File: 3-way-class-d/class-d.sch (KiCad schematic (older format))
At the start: 7 parts

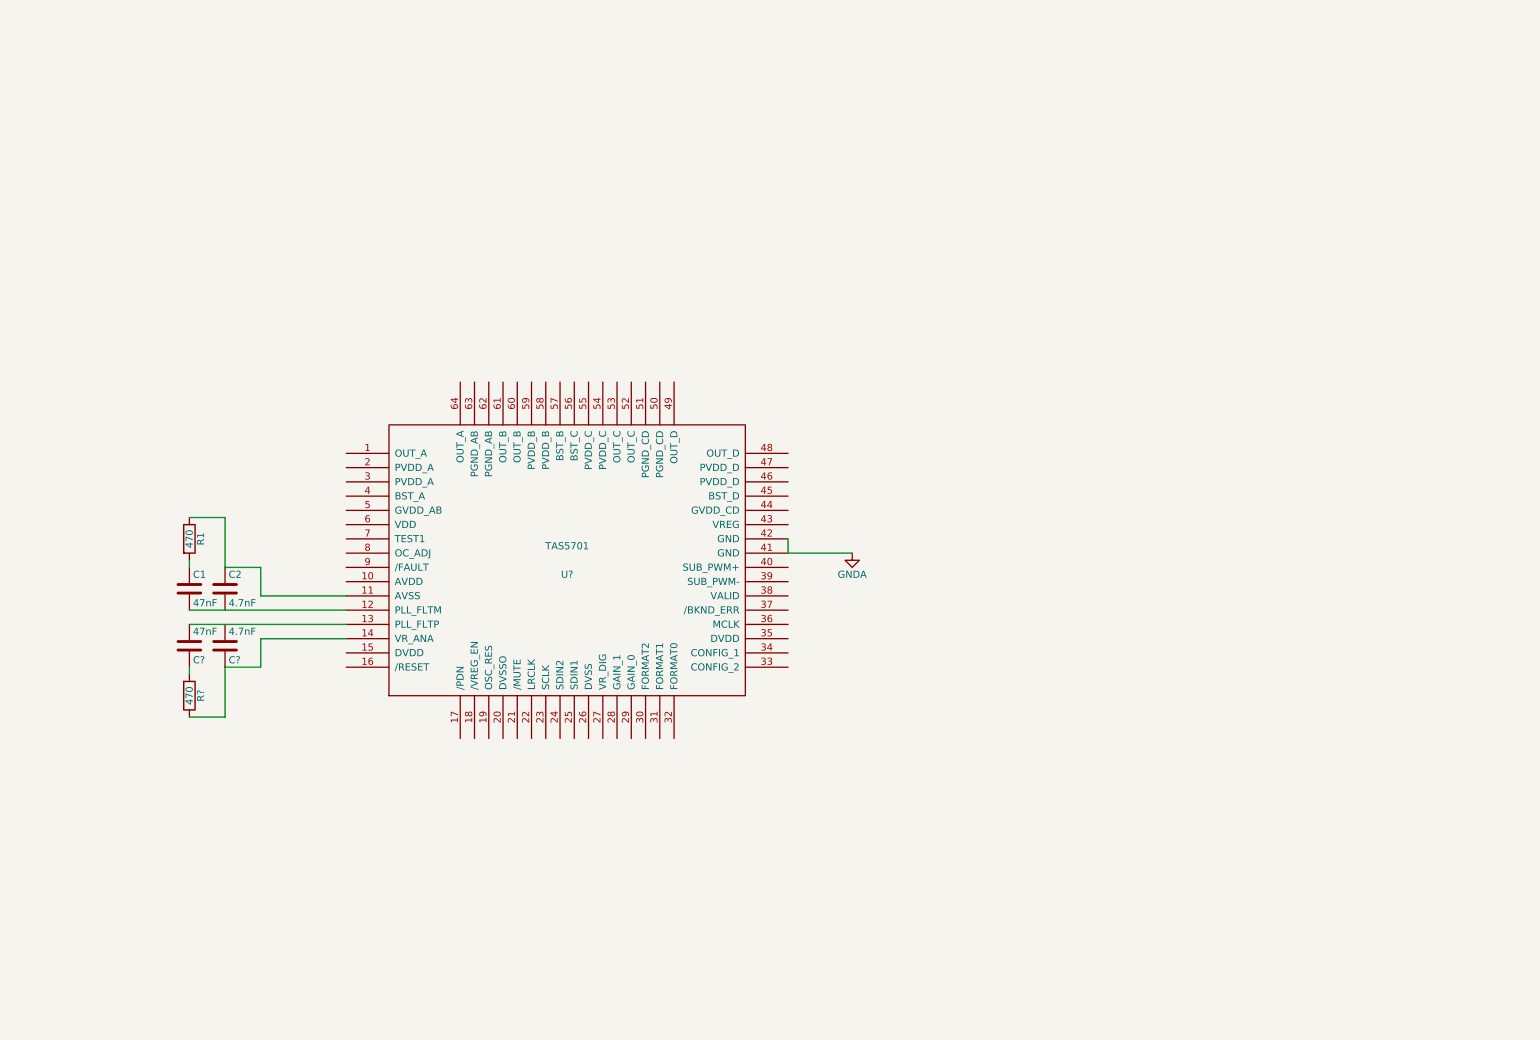
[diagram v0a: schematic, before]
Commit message: Format, gain, fault & mute LED
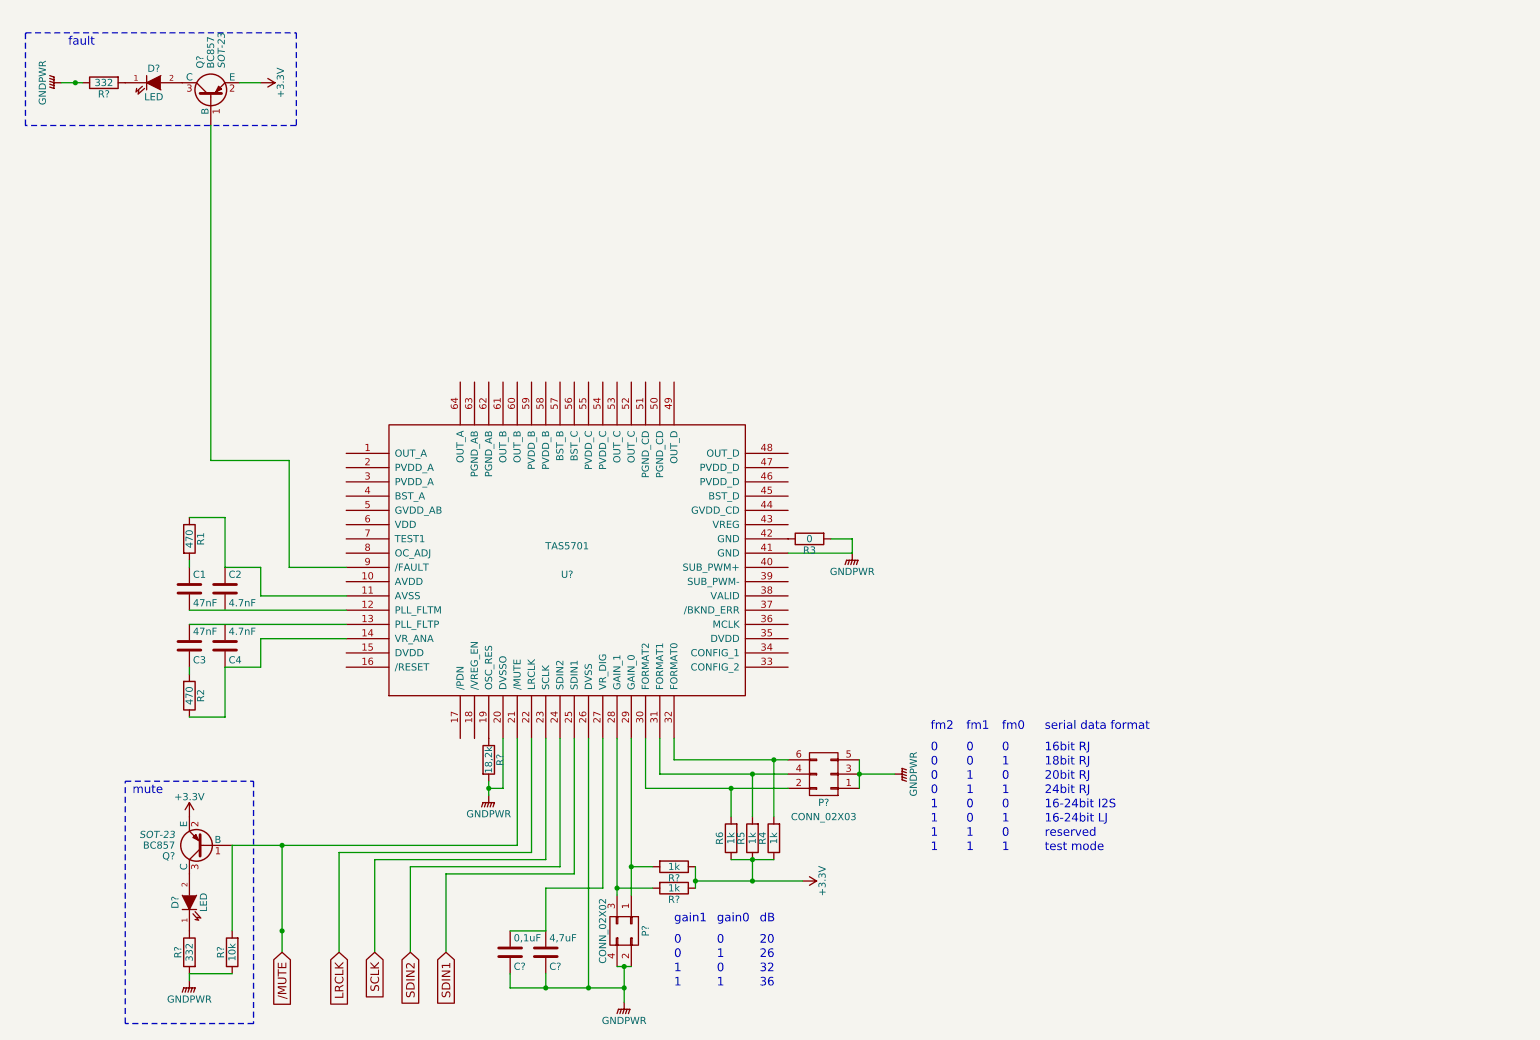
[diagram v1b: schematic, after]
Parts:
- added C?: 4,7uF, symbol C
- added C?: 0,1uF, symbol C
- added D? (x2): LED, symbol LED
- added P?: CONN_02X03, symbol CONN_02X03
- added P?: CONN_02X02, symbol CONN_02X02
- added Q? (x2): BC857, SOT-23, symbol BC857
- added R3: 0, symbol R
- added R4, R5, R6, R? (x2): 1k, symbol R
- added R? (x2): 332, symbol R
- added R?: 18,2k, symbol R
- added R?: 10k, symbol R
- gave numbers to parts that had none: 3
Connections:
- net at U?.19 (OSC_RES): now also R?.1
- net GNDPWR: now reaches U?.20 (DVSSO)
- net GNDPWR: now also U?.26 (DVSS), U?.41 (GND), C?.1, C?.1, P?.1 (P1), P?.2 (P2), P?.3 (P3), P?.4 (P4), P?.5 (P5), R3.2, R?.1, R?.1, R?.2, R?.2
- net /MUTE: now reaches U?.21 (/MUTE)
- net /MUTE: now also Q?.1 (B), R?.2
- net LRCLK: now reaches U?.22 (LRCLK)
- net SCLK: now reaches U?.23 (SCLK)
- net SDIN2: now reaches U?.24 (SDIN2)
- net SDIN1: now reaches U?.25 (SDIN1)
- net at U?.27 (VR_DIG): now also C?.2, C?.2
- net at U?.28 (GAIN_1): now also P?.3 (P3), R?.2
- net at U?.29 (GAIN_0): now also P?.1 (P1), R?.2
- net at U?.30 (FORMAT2): now also P?.2 (P2), R6.2
- net at U?.31 (FORMAT1): now also P?.4 (P4), R5.2
- net at U?.32 (FORMAT0): now also P?.6 (P6), R4.2
- net at U?.9 (/FAULT): now also Q?.1 (B)
- net GNDA: no longer names the net of U?.42 (GND)
- net GNDA: now also R3.1; no longer U?.41 (GND)
- new net: D?.2 (A), Q?.3 (C) (x2)
- new net: D?.1 (K), R?.2
- new net: D?.1 (K), R?.1
- new net +3V3: Q?.2 (E), Q?.2 (E), R4.1, R5.1, R6.1, R?.1, R?.1
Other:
- note added: "0"
- note added: "1"
- note added: "16-24bit I2S"
- note added: "16-24bit LJ"
- note added: "16bit RJ"
- note added: "18bit RJ"
- note added: "20"
- note added: "20bit RJ"
- note added: "24bit RJ"
- note added: "26"
- note added: "32"
- note added: "36"
- note added: "dB"
- note added: "fault"
- note added: "fm0"
- note added: "fm1"
- note added: "fm2"
- note added: "gain0"
- note added: "gain1"
- note added: "mute"
- note added: "reserved"
- note added: "serial data format"
- note added: "test mode"

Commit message: PVDD decoupling and output filters
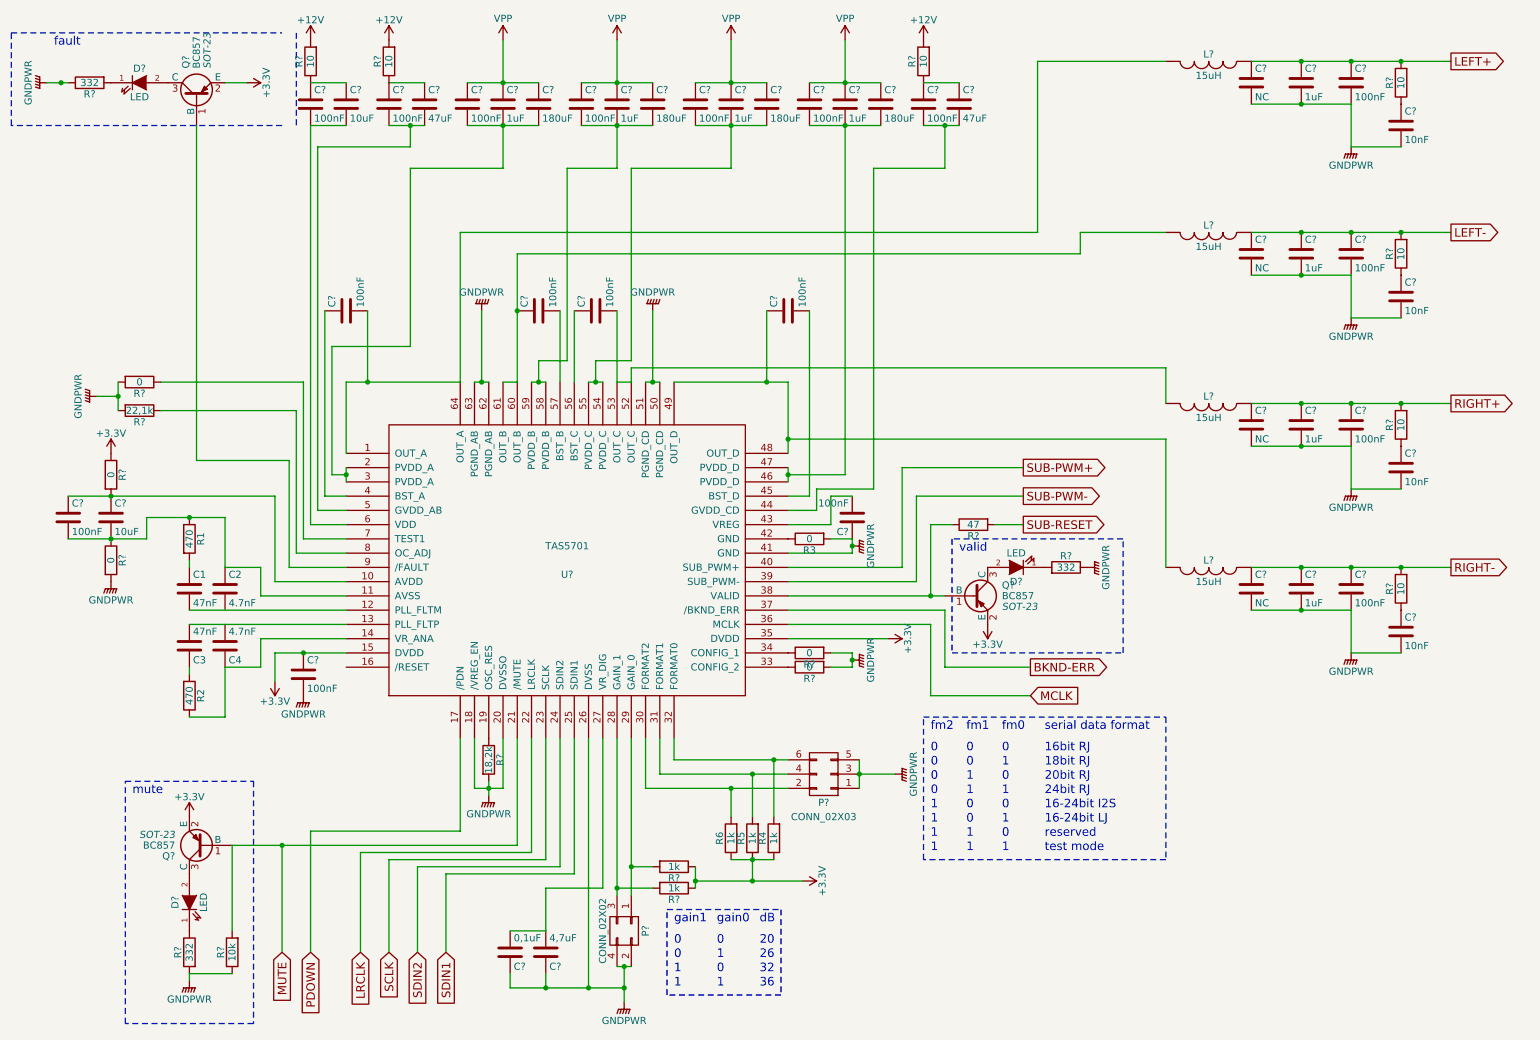
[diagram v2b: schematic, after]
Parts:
- added C? (x18): 100nF, symbol C
- added C? (x2): 10uF, symbol C
- added C? (x2): 47uF, symbol C
- added C? (x8): 1uF, symbol C
- added C? (x4): 180uF, symbol C
- added C? (x4): NC, symbol C
- added C? (x4): 10nF, symbol C
- added D?: LED, symbol LED
- added L? (x4): 15uH, symbol INDUCTOR
- added Q?: BC857, SOT-23, symbol BC857
- added R? (x5): 0, symbol R
- added R?: 22,1k, symbol R
- added R?: 332, symbol R
- added R?: 47, symbol R
- added R? (x7): 10, symbol R
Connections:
- net +3V3: now also U?.15 (DVDD), U?.35 (DVDD), C?.1, Q?.2 (E), R?.1
- net GNDPWR: now also U?.18 (/VREG_EN), U?.50 (PGND_CD), U?.51 (PGND_CD), U?.62 (PGND_AB), U?.63 (PGND_AB), C?.1, C?.2, C?.2, C?.2, C?.2, C?.2, C?.2, C?.2, C?.2, C?.2, C?.2, C?.2, C?.2, C?.2, C?.2, C?.2, C?.2, C?.2, R?.1, R?.2, R?.2, R?.2, R?.2, R?.2
- net at U?.1 (OUT_A): now also U?.64 (OUT_A), C?.2, L?.2
- net at U?.10 (AVDD): now also C?.1, C?.1, R?.2
- net at C2.1, R1.1, U?.11 (AVSS): now also C?.2, C?.2, R?.1
- net PDOWN: now reaches U?.17 (/PDN)
- net at U?.2 (PVDD_A): now also U?.3 (PVDD_A), C?.2, C?.2, C?.2
- net at U?.33 (CONFIG_2): now also R?.1
- net at U?.34 (CONFIG_1): now also R?.1
- net MCLK: now reaches U?.36 (MCLK)
- net BKND-ERR: now reaches U?.37 (/BKND_ERR)
- net at U?.38 (VALID): now also Q?.1 (B), R?.1
- net SUB-PWM-: now reaches U?.39 (SUB_PWM-)
- net at U?.4 (BST_A): now also C?.1
- net SUB-PWM+: now reaches U?.40 (SUB_PWM+)
- net at U?.43 (VREG): now also C?.2
- net at U?.44 (GVDD_CD): now also C?.2, C?.2
- net at U?.45 (BST_D): now also C?.2
- net at U?.46 (PVDD_D): now also U?.47 (PVDD_D), C?.2, C?.2, C?.2
- net at U?.48 (OUT_D): now also U?.49 (OUT_D), C?.1, L?.2
- net at U?.5 (GVDD_AB): now also C?.2, C?.2
- net at U?.52 (OUT_C): now also U?.53 (OUT_C), C?.2, L?.2
- net at U?.54 (PVDD_C): now also U?.55 (PVDD_C), C?.2, C?.2, C?.2
- net at U?.56 (BST_C): now also C?.1
- net at U?.57 (BST_B): now also C?.2
- net at U?.58 (PVDD_B): now also U?.59 (PVDD_B), C?.2, C?.2, C?.2
- net at U?.6 (VDD): now also C?.2, C?.2
- net at U?.60 (OUT_B): now also U?.61 (OUT_B), C?.1, L?.2
- net at U?.7 (TEST1): now also R?.1
- net at U?.8 (OC_ADJ): now also R?.1
- net /MUTE renamed MUTE
- new net: D?.2 (A), Q?.3 (C)
- new net: D?.1 (K), R?.2
- new net: C?.1, C?.1, R?.1 (x3)
- new net: C?.1, R?.1 (x4)
- new net +12V: R?.2, R?.2, R?.2
- new net LEFT+: C?.1, C?.1, C?.1, L?.1, R?.2
- new net LEFT-: C?.1, C?.1, C?.1, L?.1, R?.2
- new net RIGHT+: C?.1, C?.1, C?.1, L?.1, R?.2
- new net RIGHT-: C?.1, C?.1, C?.1, L?.1, R?.2
- new net SUB-RESET: R?.2
- new net VPP: C?.1, C?.1, C?.1, C?.1, C?.1, C?.1, C?.1, C?.1, C?.1, C?.1, C?.1, C?.1
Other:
- note added: "valid"
- moved on the sheet: D?, Q?, R?
